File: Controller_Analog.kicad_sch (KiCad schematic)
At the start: 28 parts, among them J1 Conn_01x02, J2 Conn_01x05, J3 Conn_01x05, U1 OP07, U2 OP07, U3 OP07, U4 NJM4191M

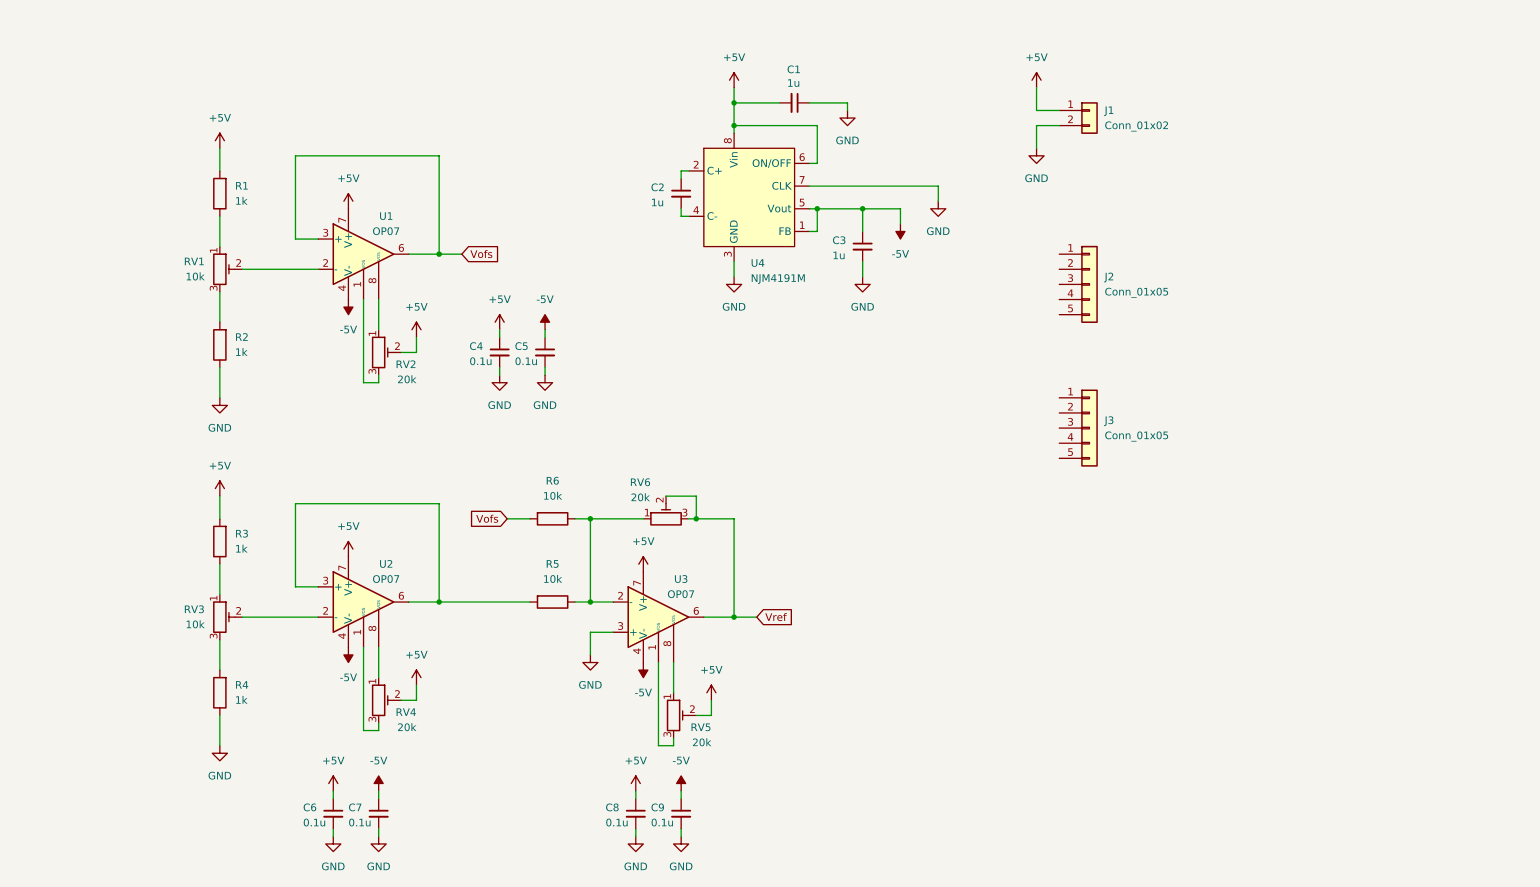
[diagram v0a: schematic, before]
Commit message: add Universal Board version
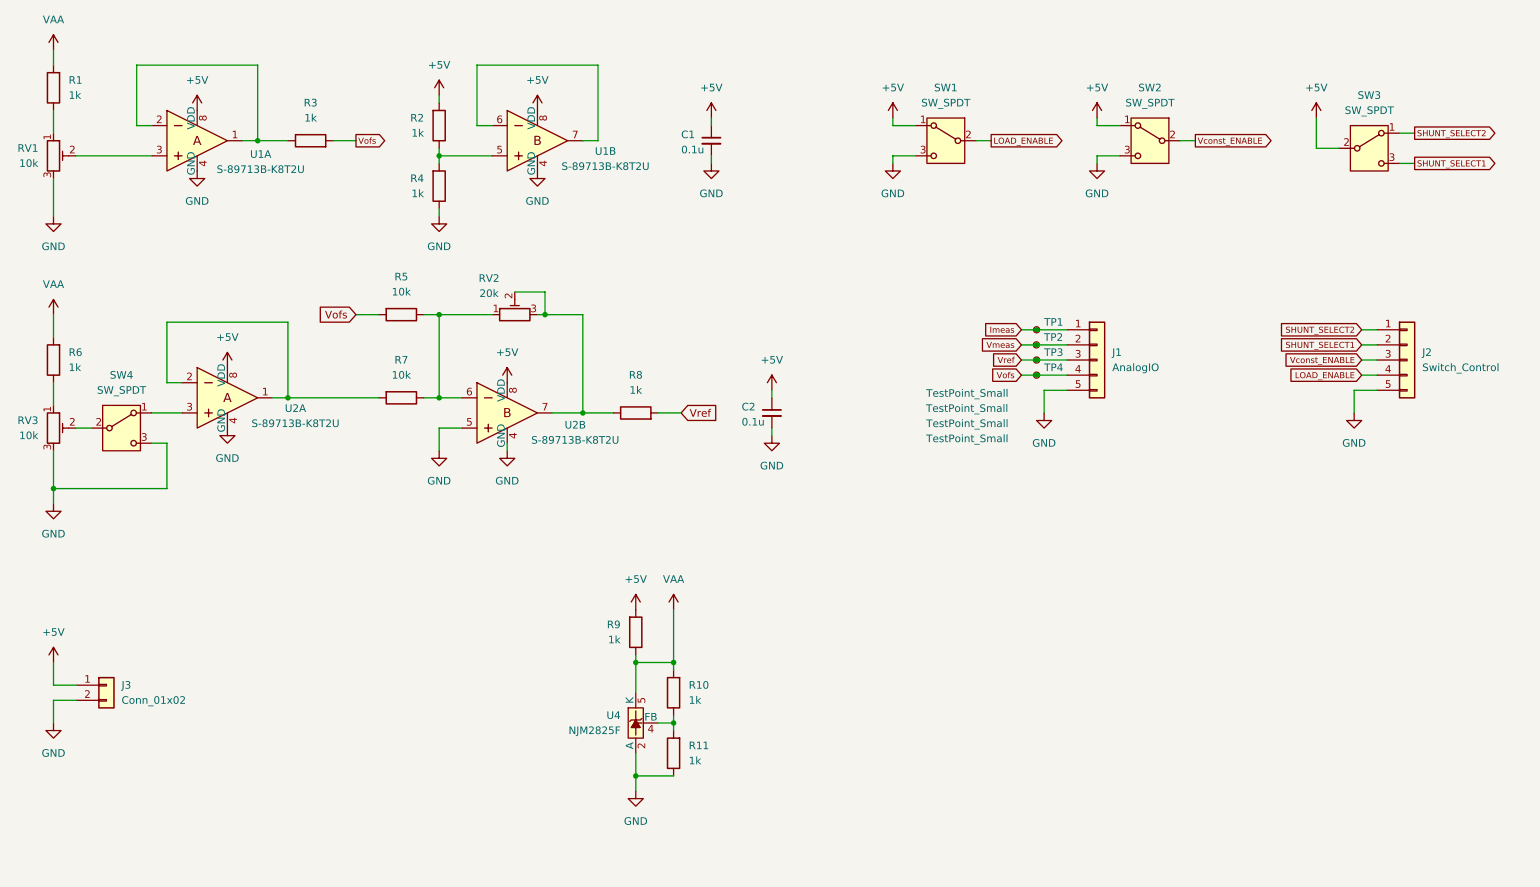
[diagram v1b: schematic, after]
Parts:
- removed C1, C2, C3: 1u, Capacitor_THT:C_Disc_D4.7mm_W2.5mm_P5.00mm, symbol Device:C_Small
- removed C5, C6, C7, C9: 0.1u, Capacitor_THT:C_Disc_D4.7mm_W2.5mm_P5.00mm, symbol Device:C_Small
- removed RV2, RV4, RV5: 20k, Potentiometer_THT:Potentiometer_Vishay_T73YP_Vertical, symbol Device:R_Potentiometer_Trim
- removed U1, U2, U3: OP07, Package_DIP:DIP-8_W7.62mm, symbol Amplifier_Operational:OP07
- removed U4: NJM4191M, Package_DIP:DIP-8_W7.62mm, symbol AM_PowerIC_Switching:NJM4191M
- added R10, R11, R3, R8, R9: 1k, Inductor_THT:L_Axial_L5.3mm_D2.2mm_P10.16mm_Horizontal_Vishay_IM-1, symbol Device:R
- added SW1, SW4: SW_SPDT, AM_Switch:2MS1-T1-B4-M2-Q-E, symbol Switch:SW_SPDT
- added SW2, SW3: SW_SPDT, AM_Switch: SS-12D00G3, symbol Switch:SW_SPDT
- added TP1, TP2, TP3, TP4: TestPoint_Small, TestPoint:TestPoint_THTPad_D2.0mm_Drill1.0mm, symbol Connector:TestPoint_Small
- added U1, U2: S-89713B-K8T2U, Package_DIP:DIP-8_W7.62mm_Socket, symbol AM_Opamp:S-89713B-K8T2U
- added U4: NJM2825F, Package_DIP:DIP-6_W7.62mm_Socket, symbol AM_PowerIC_Linear:NJM2825F
- J1: renamed from J2; value Conn_01x05 -> AnalogIO; footprint (none) -> Connector_JST:JST_XH_B5B-XH-A_1x05_P2.50mm_Vertical
- J2: renamed from J3; value Conn_01x05 -> Switch_Control; footprint (none) -> Connector_JST:JST_XH_B5B-XH-A_1x05_P2.50mm_Vertical
- R1, R2, R4: footprint Resistor_THT:R_Axial_DIN0207_L6.3mm_D2.5mm_P10.16mm_Horizontal -> Inductor_THT:L_Axial_L5.3mm_D2.2mm_P10.16mm_Horizontal_Vishay_IM-1
- R5: renamed from R6; footprint Resistor_THT:R_Axial_DIN0207_L6.3mm_D2.5mm_P10.16mm_Horizontal -> Inductor_THT:L_Axial_L5.3mm_D2.2mm_P10.16mm_Horizontal_Vishay_IM-1
- R6: renamed from R3; footprint Resistor_THT:R_Axial_DIN0207_L6.3mm_D2.5mm_P10.16mm_Horizontal -> Inductor_THT:L_Axial_L5.3mm_D2.2mm_P10.16mm_Horizontal_Vishay_IM-1
- R7: renamed from R5; footprint Resistor_THT:R_Axial_DIN0207_L6.3mm_D2.5mm_P10.16mm_Horizontal -> Inductor_THT:L_Axial_L5.3mm_D2.2mm_P10.16mm_Horizontal_Vishay_IM-1
- renumbered C4 to C1, C8 to C2, J1 to J3, RV6 to RV2
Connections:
- net +5V: now also R2.2, R9.2, SW1.1 (A), SW2.1 (A), SW3.2 (B), U1.8 (VDD), U1.8 (VDD), U2.8 (VDD), U2.8 (VDD); no longer R1.2, R6.2
- net GND: now also J1.5 (Pin_5), J2.5 (Pin_5), RV1.3, RV3.3, R11.1, SW1.3 (C), SW2.3 (C), SW4.3 (C), U1.4 (GND), U1.4 (GND), U2.4 (GND), U2.4 (GND), U2.5, U4.2 (A); no longer R2.1
- net Vofs: now also J1.4 (Pin_4), R3.2, TP4.1
- net Vref: now also J1.3 (Pin_3), R8.2, TP3.1; no longer RV2.2, RV2.3
- net Imeas: now reaches J1.1 (Pin_1)
- net Imeas: now also TP1.1
- net Vmeas: now reaches J1.2 (Pin_2)
- net Vmeas: now also TP2.1
- net at R5.1, R7.1, RV2.1: now also U2.6
- net at R7.2: now also U2.1, U2.2
- net at RV3.2: now also SW4.2 (B)
- net at RV1.2: now also U1.3
- net at R4.2: now also R2.1, U1.5; no longer RV3.3
- net SHUNT_SELECT2: now reaches J2.1 (Pin_1)
- net SHUNT_SELECT2: now also SW3.1 (A)
- net SHUNT_SELECT1: now reaches J2.2 (Pin_2)
- net SHUNT_SELECT1: now also SW3.3 (C)
- net Vconst_ENABLE: now reaches J2.3 (Pin_3)
- net Vconst_ENABLE: now also SW2.2 (B)
- net LOAD_ENABLE: now reaches J2.4 (Pin_4)
- net LOAD_ENABLE: now also SW1.2 (B)
- new net: R10.1, R11.2, U4.4 (FB)
- new net: R8.1, RV2.2, RV2.3, U2.7
- new net: SW4.1 (A), U2.3
- new net: R3.1, U1.1, U1.2
- new net: U1.6, U1.7
- new net VAA: R1.2, R10.2, R6.2, R9.1, U4.5 (K)
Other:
- moved on the sheet: C1, C2, J1, J2, J3, R1, R5, R6, R7, RV1, RV2, RV3

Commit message: wired components
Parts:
- added H1, H2, H3, H4: MountingHole, MountingHole:MountingHole_3.2mm_M3, symbol Mechanical:MountingHole
- added P1: Eoshi-chan_Silk, Eoshi-chan_v2:Eoshi-chan-v2_10x10, symbol Eoshi-chan:Eoshi-chan_Silk
- C1, C2: footprint Capacitor_THT:C_Disc_D4.7mm_W2.5mm_P5.00mm -> Capacitor_SMD:C_0603_1608Metric
- R1, R2, R3, R4, R6, R8: footprint Inductor_THT:L_Axial_L5.3mm_D2.2mm_P10.16mm_Horizontal_Vishay_IM-1 -> Resistor_SMD:R_0603_1608Metric
- R10, R11, R5, R7, R9: footprint Inductor_THT:L_Axial_L5.3mm_D2.2mm_P10.16mm_Horizontal_Vishay_IM-1 -> Resistor_THT:R_Axial_DIN0207_L6.3mm_D2.5mm_P10.16mm_Horizontal
- RV3: footprint Potentiometer_THT:Potentiometer_Vishay_T73YP_Vertical -> Potentiometer_THT:Potentiometer_Alps_RK09K_Single_Vertical
- U1, U2: footprint Package_DIP:DIP-8_W7.62mm_Socket -> Package_SO:MSOP-8_3x3mm_P0.65mm
- U4: footprint Package_DIP:DIP-6_W7.62mm_Socket -> Package_TO_SOT_SMD:SOT-23-5
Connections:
- net +5V: now also SW1.3 (C); no longer SW1.1 (A)
- net GND: now also SW1.1 (A); no longer SW1.3 (C)
- net at R5.1, R7.1, U2.6: now also RV2.3; no longer RV2.1
- net at R8.1, RV2.2, U2.7: now also RV2.1; no longer RV2.3
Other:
- moved on the sheet: RV2, SW1
